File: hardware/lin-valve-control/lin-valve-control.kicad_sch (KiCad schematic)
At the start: 14 parts, among them Q1 SUD50P04-08, Q2 2N7002, Q3 SUD50P04-08, Q4 2N7002, U1 Arduino_Nano_v3.x

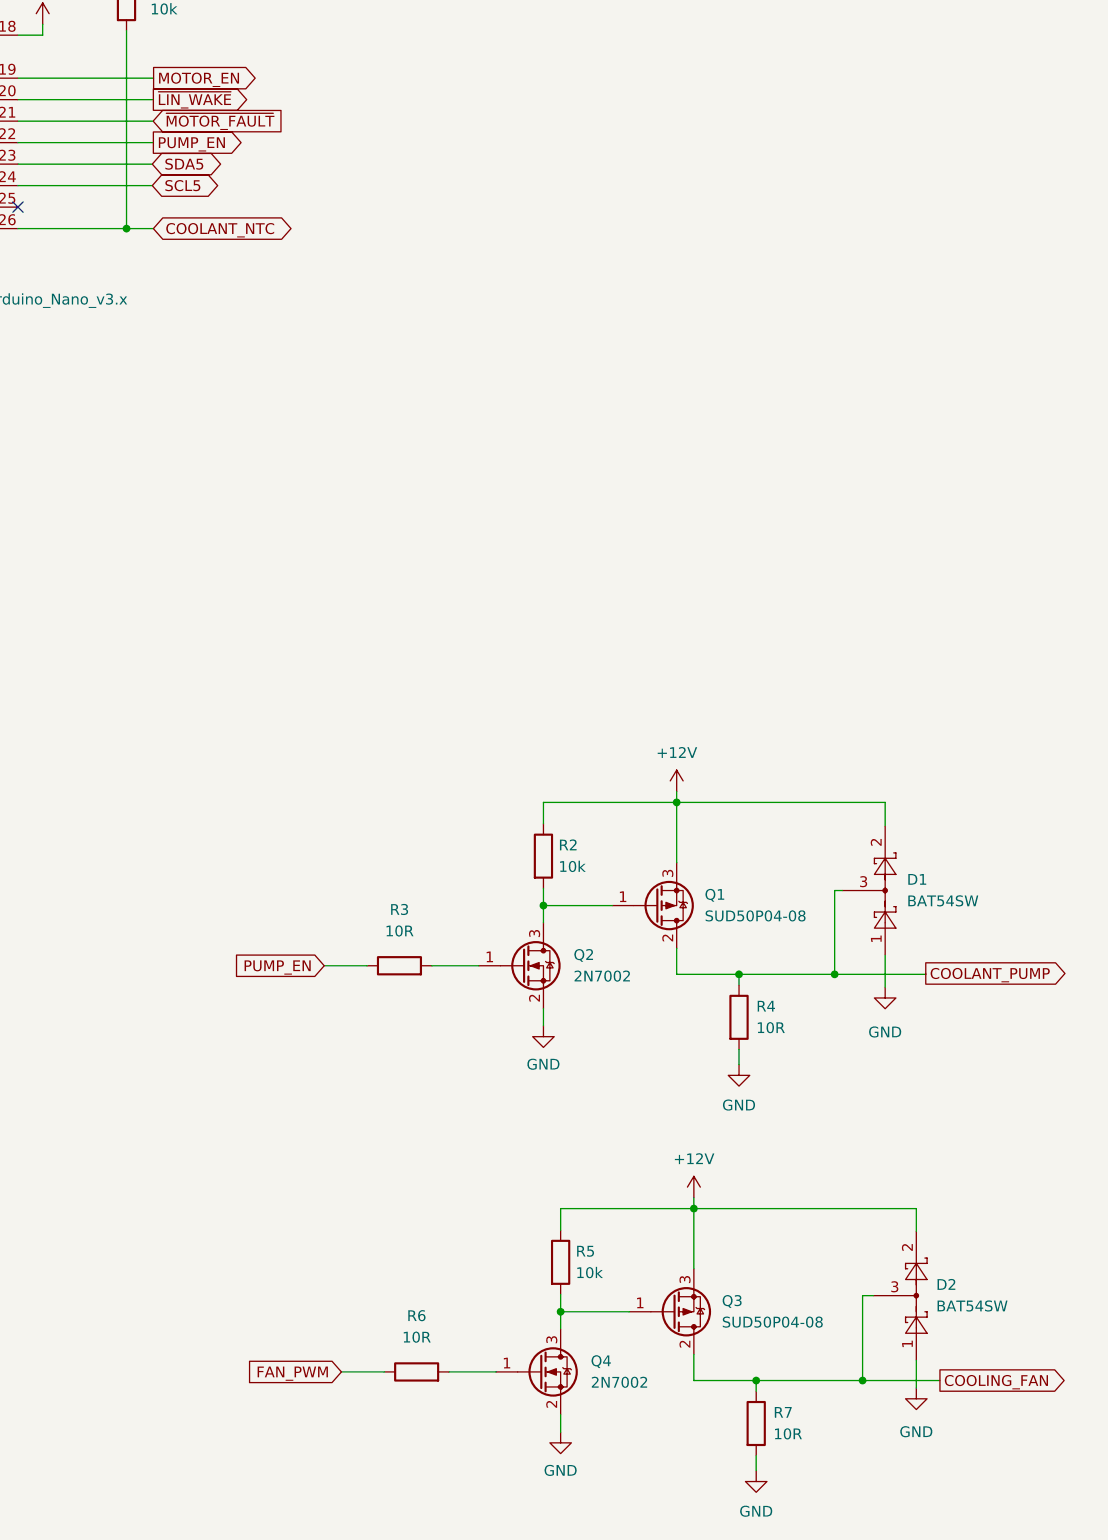
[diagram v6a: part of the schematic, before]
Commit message: Updated valve controller board
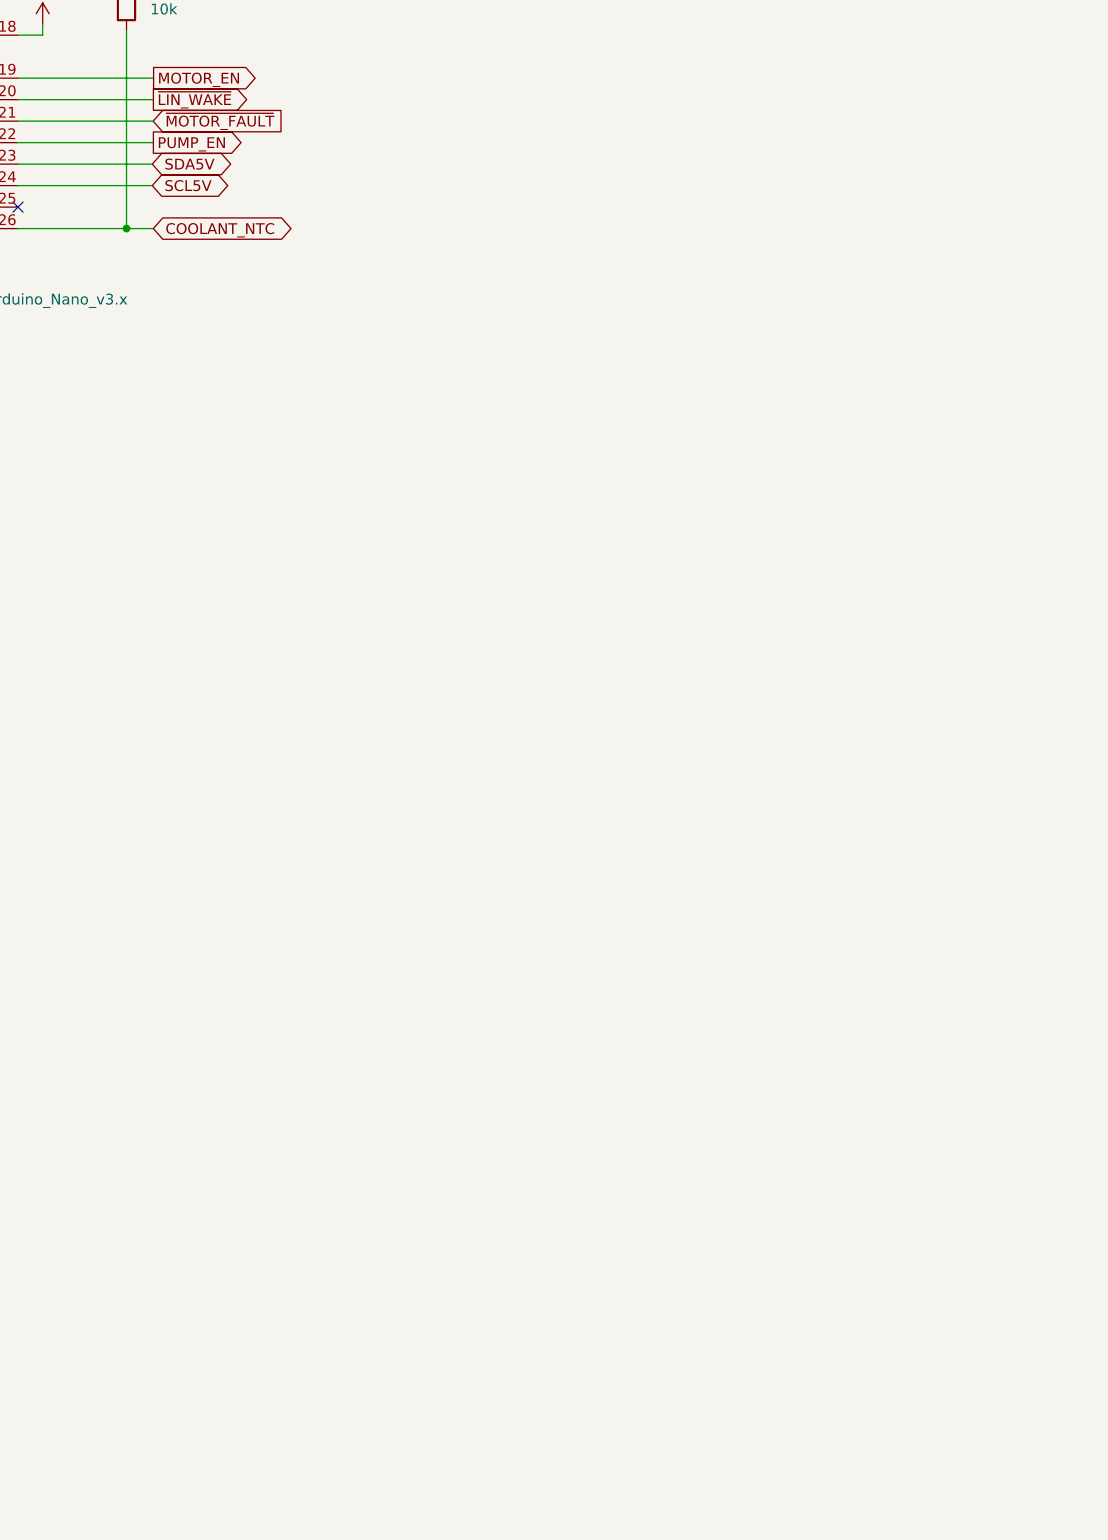
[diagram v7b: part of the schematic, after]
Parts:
- removed D1, D2: BAT54SW, Package_TO_SOT_SMD:SOT-323_SC-70, symbol Diode:BAT54SW
- removed Q1, Q3: SUD50P04-08, Package_TO_SOT_SMD:TO-252-2, symbol Transistor_FET:SUD50P04-08
- removed Q2, Q4: 2N7002, Package_TO_SOT_SMD:SOT-23, symbol Transistor_FET:2N7002
- removed R2, R5: 10k, Resistor_SMD:R_0805_2012Metric_Pad1.20x1.40mm_HandSolder, symbol Device:R
- removed R3, R4, R6, R7: 10R, Resistor_SMD:R_0805_2012Metric_Pad1.20x1.40mm_HandSolder, symbol Device:R
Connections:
- net SCL5 renamed SCL5V
- net SDA5 renamed SDA5V
